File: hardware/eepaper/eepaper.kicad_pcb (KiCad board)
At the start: 4 copper layers, 58.4 x 35.6 mm, 63 parts, among them J1 S2B-PH-SM4-TB, J2 USB4105-GF-A, J3 105162-0001, J4 FFC2B28-24-G, J5 Conn_01x19, Q1 SI2305-TP, Q2 PJC7400_R1_00001, U1 MCP73831-2-OT, U2 RT9080-33GJ5, U3 ESP32-C3-WROOM-02-H4

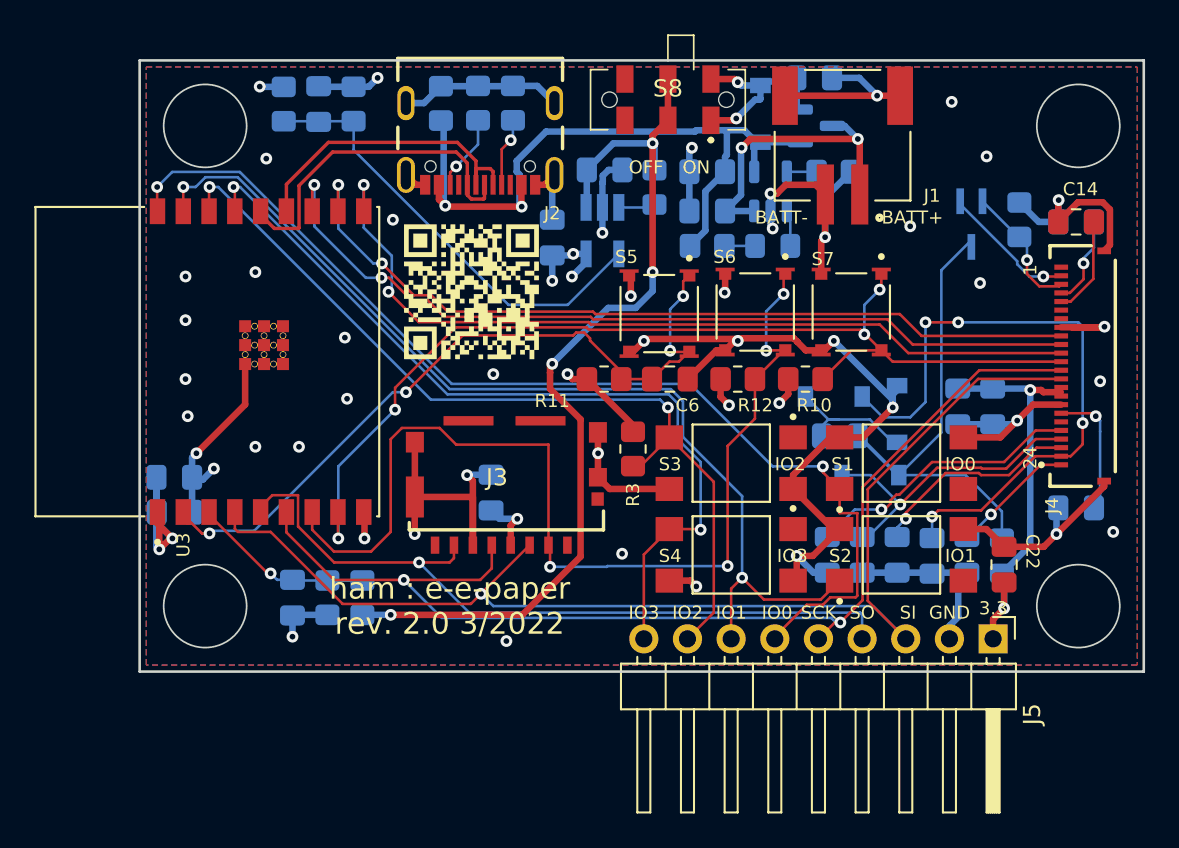
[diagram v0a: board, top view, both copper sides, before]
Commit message: Add v2 hardware files sent to fabrication
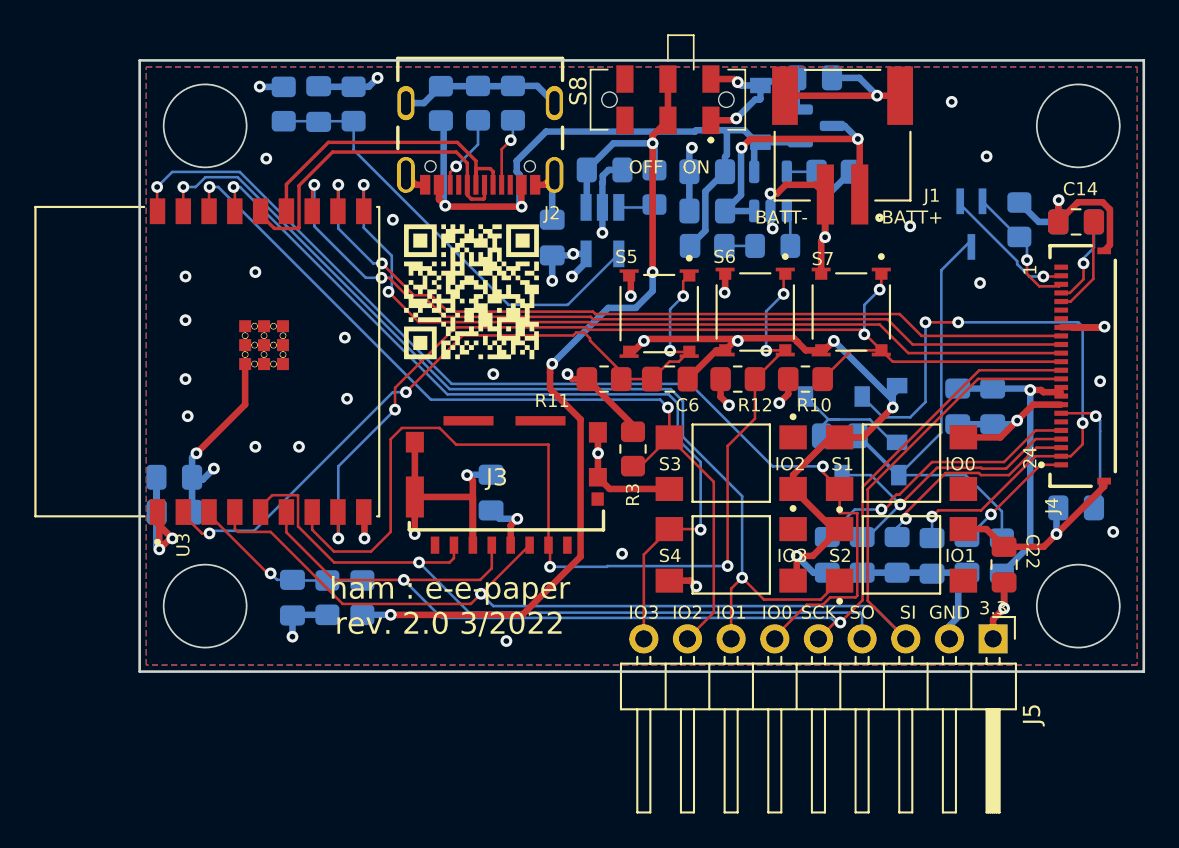
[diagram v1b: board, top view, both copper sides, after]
